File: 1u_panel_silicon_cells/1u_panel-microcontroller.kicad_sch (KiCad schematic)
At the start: 33 parts, among them J2 2-1734592-0, U1 TCAN330GDCNT, U11 TMP101NA/3KSLOTTED, U2 TMP101NA/3KSLOTTED, U7 STM32F091CCT7, X1 ECS-160-10-36Q-ES-TR

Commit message: changes for silicon solar module bringup tasks
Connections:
- net 3.3V: now also U11.4 (V+), U11.5 (ADD0), U2.4 (V+); no longer U11.1 (V+), U11.2 (ADD0), U2.1 (V+)
- net GND: now also U11.2 (GND); no longer U11.5 (GND)
- net SCL: now also U11.1 (SCL), U2.1 (SCL); no longer U11.4 (SCL), U2.4 (SCL)
- net SDA: now also U11.6 (SDA), U2.6 (SDA); no longer U11.3 (SDA), U2.3 (SDA)
- net at TP4.1: now also U2.3 (ALERT); no longer U2.6 (ALERT)
- net at TP30.1: now also U11.3 (ALERT); no longer U11.6 (ALERT)

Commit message: chages for https://github.com/oresat/oresat-solar-hardware/issues/53
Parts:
- U1: footprint oresat-ics:SOT23-8_TI-DCN -> Package_TO_SOT_SMD:SOT-23-8
- U11, U2: symbol oresat-ics:TMP101NA -> Sensor_Temperature:TMP101
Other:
- moved on the sheet: TP30, TP4

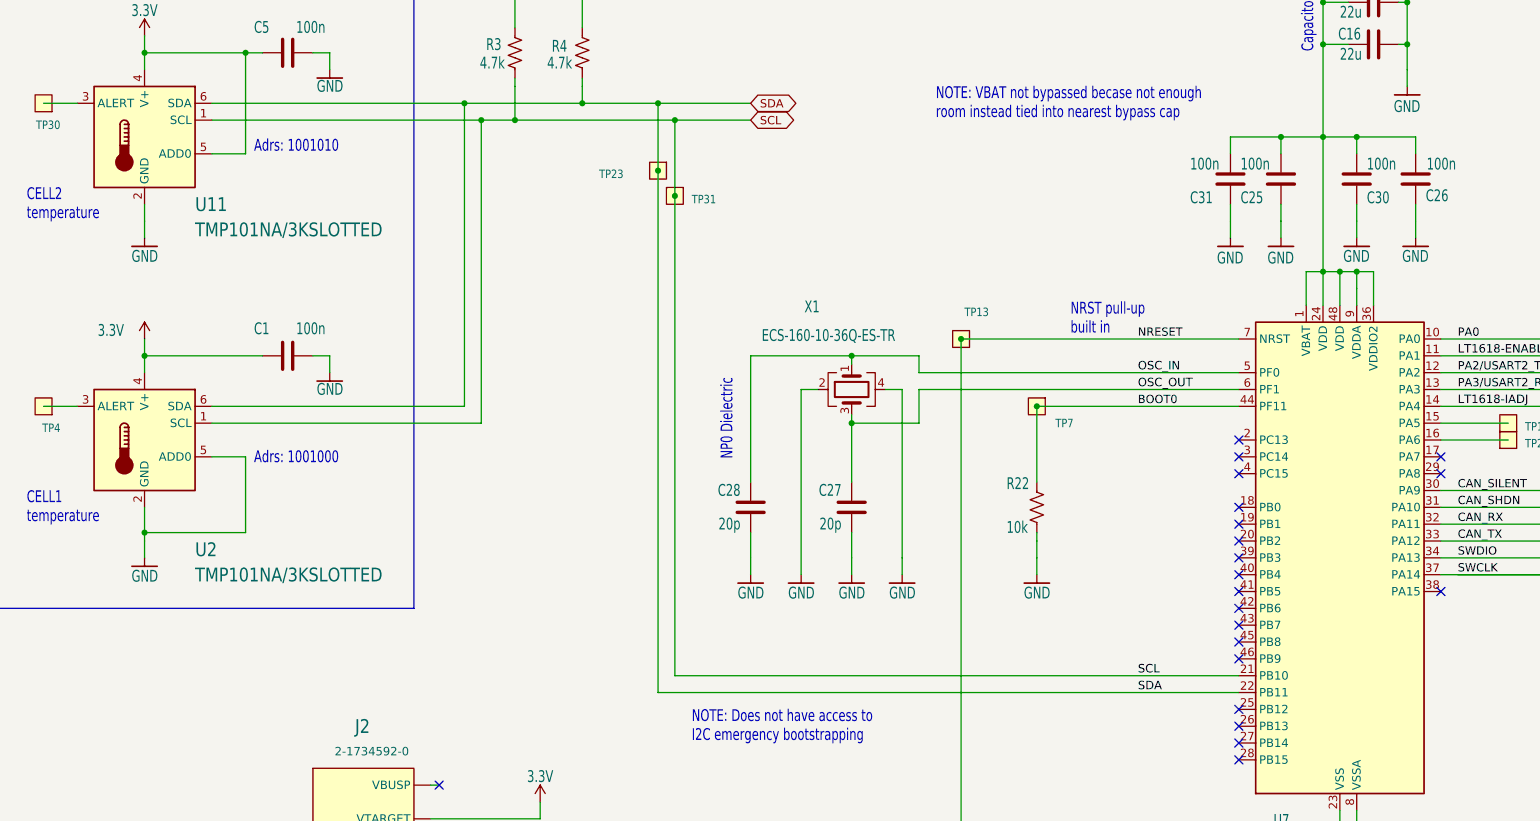
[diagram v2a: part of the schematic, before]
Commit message: changes for bringup issues on Si Solar module
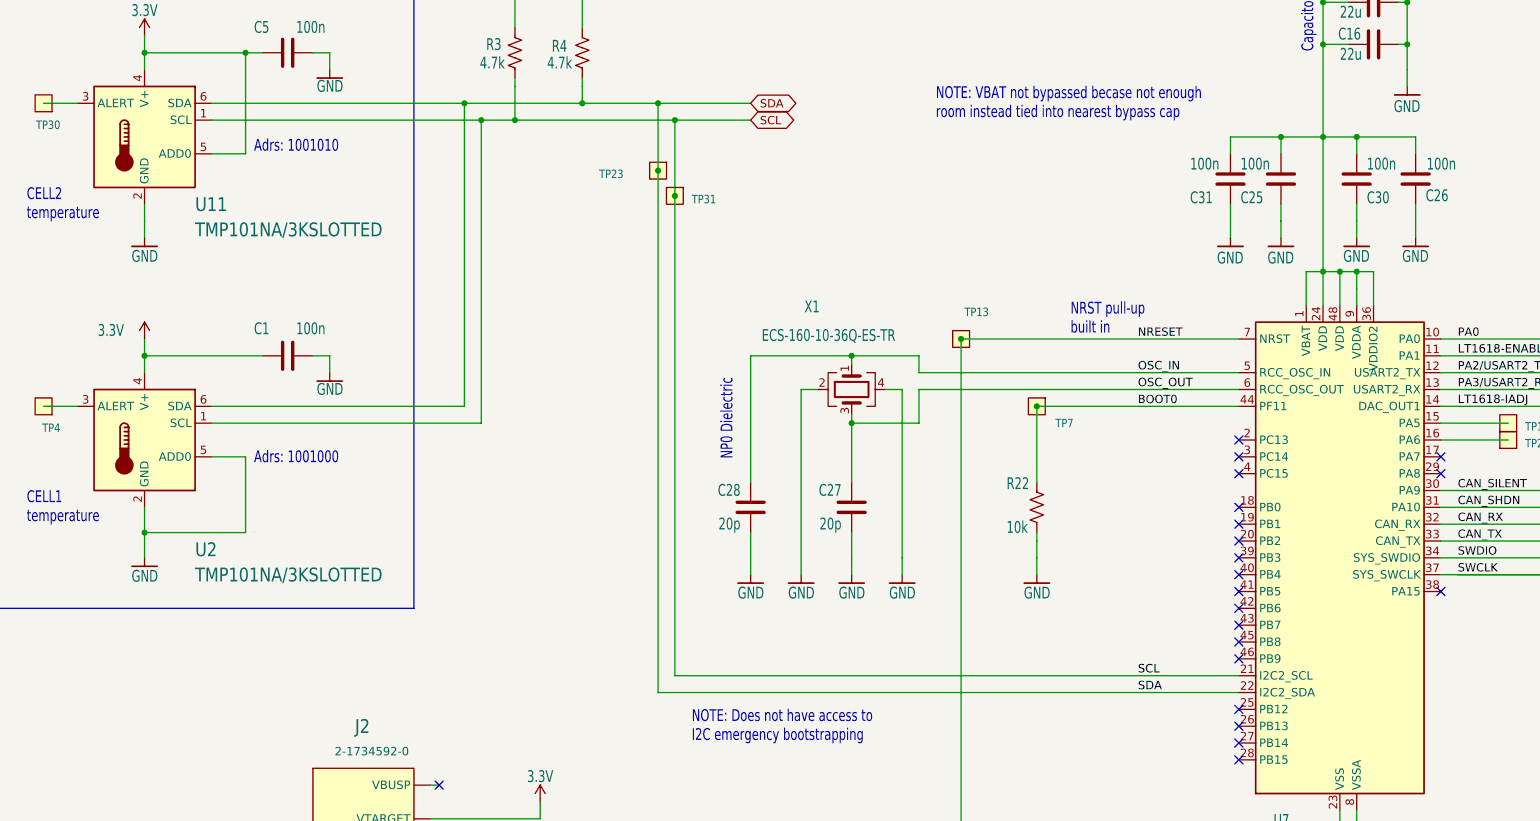
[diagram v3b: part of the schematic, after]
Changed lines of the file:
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@@
 (kicad_sch
-	(version 20231120)
+	(version 20250114)
 	(generator "eeschema")
-	(generator_version "8.0")
+	(generator_version "9.0")
 	(paper "USLedger")
 	(title_block
@@
 		(rev "1.0")
 	)
+	(text "Capacitor bank"
+		(exclude_from_sim no)
+		(at 243.84 50.8 90)
+		(effects
+			(font
+				(size 1.778 1.27)
+			)
+			(justify left bottom)
+		)
+	)
+	(text "Temp Sensors"
+		(exclude_from_sim no)
+		(at 58.42 38.1 0)
+		(effects
+			(font
+				(size 3.81 3.2385)
+				(thickness 0.6477)
+				(bold yes)
+			)
+			(justify left bottom)
+		)
+	)
+	(text "NOTE: VBAT not bypassed becase not enough\nroom instead tied into nearest bypass cap"
+		(exclude_from_sim no)
+		(at 186.69 60.96 0)
+		(effects
+			(font
+				(size 1.778 1.27)
+			)
+			(justify left bottom)
+		)
+	)
+	(text "DNP\nFOR\nFLIGHT"
+		(exclude_from_sim no)
+		(at 318.008 105.156 0)
+		(effects
+			(font
+				(size 1.778 1.27)
+			)
+			(justify left bottom)
+		)
+	)
+	(text "NRST pull-up\nbuilt in"
+		(exclude_from_sim no)
+		(at 207.01 93.472 0)
+		(effects
+			(font
+				(size 1.778 1.27)
+			)
+			(justify left bottom)
+		)
+	)
+	(text "DNP\nFOR\nFLIGHT"
+		(exclude_from_sim no)
+		(at 302.26 91.44 0)
+		(effects
+			(font
+				(size 1.778 1.27)
+			)
+			(justify left bottom)
+		)
+	)
+	(text "CAN Transceiver"
+		(exclude_from_sim no)
+		(at 365.76 88.9 0)
+		(effects
+			(font
+				(size 2.54 2.159)
+				(thickness 0.4318)
+				(bold yes)
+			)
+			(justify right bottom)
+		)
+	)
+	(text "NP0 Dielectric"
+		(exclude_from_sim no)
+		(at 156.21 112.268 90)
+		(effects
+			(font
+				(size 1.778 1.27)
+			)
+			(justify left bottom)
+		)
+	)
+	(text "NOTE: DEBUG-1 powers solar module\n3.3V directly from FT23X's onboard\nLDO on the DEBUG board. Schottky\ndiode drops 3.3V LDO output to 3.0V;\nkicking in solar should be  fine since\n3.3 V > 3.0V which the diode will\nblock."
+		(exclude_from_sim no)
+		(at 134.62 210.82 0)
+		(effects
+			(font
+				(size 1.778 1.27)
+			)
+			(justify left bottom)
+		)
+	)
+	(text "Adrs: 1001010"
+		(exclude_from_sim no)
+		(at 83.82 66.04 0)
+		(effects
+			(font
+				(size 1.778 1.27)
+			)
+			(justify left bottom)
+		)
+	)
+	(text "Adrs: 1001000"
+		(exclude_from_sim no)
+		(at 83.82 113.03 0)
+		(effects
+			(font
+				(size 1.778 1.27)
+			)
+			(justify left bottom)
+		)
+	)
+	(text "CELL2\ntemperature"
+		(exclude_from_sim no)
+		(at 49.53 76.2 0)
+		(effects
+			(font
+				(size 1.778 1.27)
+			)
+			(justify left bottom)
+		)
+	)
+	(text "RX-TX cross on\nDEBUG board"
+		(exclude_from_sim no)
+		(at 72.39 186.69 0)
+		(effects
+			(font
+				(size 1.778 1.27)
+			)
+			(justify left bottom)
+		)
+	)
+	(text "NOTE: Does not have access to\nI2C emergency bootstrapping"
+		(exclude_from_sim no)
+		(at 149.86 154.94 0)
+		(effects
+			(font
+				(size 1.778 1.27)
+			)
+			(justify left bottom)
+		)
+	)
+	(text "CELL1\ntemperature"
+		(exclude_from_sim no)
+		(at 49.53 121.92 0)
+		(effects
+			(font
+				(size 1.778 1.27)
+			)
+			(justify left bottom)
+		)
+	)
+	(text "0805"
+		(exclude_from_sim no)
+		(at 120.65 213.36 0)
+		(effects
+			(font
+				(size 1.778 1.27)
+			)
+			(justify left bottom)
+		)
+	)
 	(junction
 		(at 257.81 43.18)
@@
 		)
 	)
-	(text "Capacitor bank"
-		(exclude_from_sim no)
-		(at 243.84 50.8 90)
-		(effects
-			(font
-				(size 1.778 1.27)
-			)
-			(justify left bottom)
-		)
-	)
-	(text "Temp Sensors"
-		(exclude_from_sim no)
-		(at 58.42 38.1 0)
-		(effects
-			(font
-				(size 3.81 3.2385)
-				(thickness 0.6477)
-				(bold yes)
-			)
-			(justify left bottom)
-		)
-	)
-	(text "NOTE: VBAT not bypassed becase not enough\nroom instead tied into nearest bypass cap"
-		(exclude_from_sim no)
-		(at 186.69 60.96 0)
-		(effects
-			(font
-				(size 1.778 1.27)
-			)
-			(justify left bottom)
-		)
-	)
-	(text "DNP\nFOR\nFLIGHT"
-		(exclude_from_sim no)
-		(at 318.008 105.156 0)
-		(effects
-			(font
-				(size 1.778 1.27)
-			)
-			(justify left bottom)
-		)
-	)
-	(text "NRST pull-up\nbuilt in"
-		(exclude_from_sim no)
-		(at 207.01 93.472 0)
-		(effects
-			(font
-				(size 1.778 1.27)
-			)
-			(justify left bottom)
-		)
-	)
-	(text "DNP\nFOR\nFLIGHT"
-		(exclude_from_sim no)
-		(at 302.26 91.44 0)
-		(effects
-			(font
-				(size 1.778 1.27)
-			)
-			(justify left bottom)
-		)
-	)
-	(text "CAN Transceiver"
-		(exclude_from_sim no)
-		(at 365.76 88.9 0)
-		(effects
-			(font
-				(size 2.54 2.159)
-				(thickness 0.4318)
-				(bold yes)
-			)
-			(justify right bottom)
-		)
-	)
-	(text "NP0 Dielectric"
-		(exclude_from_sim no)
-		(at 156.21 112.268 90)
-		(effects
-			(font
-				(size 1.778 1.27)
-			)
-			(justify left bottom)
-		)
-	)
-	(text "NOTE: DEBUG-1 powers solar module\n3.3V directly from FT23X's onboard\nLDO on the DEBUG board. Schottky\ndiode drops 3.3V LDO output to 3.0V;\nkicking in solar should be  fine since\n3.3 V > 3.0V which the diode will\nblock."
-		(exclude_from_sim no)
-		(at 134.62 210.82 0)
-		(effects
-			(font
-				(size 1.778 1.27)
-			)
-			(justify left bottom)
-		)
-	)
-	(text "Adrs: 1001010"
-		(exclude_from_sim no)
-		(at 83.82 66.04 0)
-		(effects
-			(font
-				(size 1.778 1.27)
-			)
-			(justify left bottom)
-		)
-	)
-	(text "Adrs: 1001000"
-		(exclude_from_sim no)
-		(at 83.82 113.03 0)
-		(effects
-			(font
-				(size 1.778 1.27)
-			)
-			(justify left bottom)
-		)
-	)
-	(text "CELL2\ntemperature"
-		(exclude_from_sim no)
-		(at 49.53 76.2 0)
-		(effects
-			(font
-				(size 1.778 1.27)
-			)
-			(justify left bottom)
-		)
-	)
-	(text "RX-TX cross on\nDEBUG board"
-		(exclude_from_sim no)
-		(at 72.39 186.69 0)
-		(effects
-			(font
-				(size 1.778 1.27)
-			)
-			(justify left bottom)
-		)
-	)
-	(text "NOTE: Does not have access to\nI2C emergency bootstrapping"
-		(exclude_from_sim no)
-		(at 149.86 154.94 0)
-		(effects
-			(font
-				(size 1.778 1.27)
-			)
-			(justify left bottom)
-		)
-	)
-	(text "CELL1\ntemperature"
-		(exclude_from_sim no)
-		(at 49.53 121.92 0)
-		(effects
-			(font
-				(size 1.778 1.27)
-			)
-			(justify left bottom)
-		)
-	)
-	(text "0805"
-		(exclude_from_sim no)
-		(at 120.65 213.36 0)
-		(effects
-			(font
-				(size 1.778 1.27)
-			)
-			(justify left bottom)
-		)
-	)
 	(label "CAN_TX"
 		(at 265.43 124.46 0)
@@
 		(mirror x)
 		(unit 1)
-		(exclude_from_sim yes)
+		(exclude_from_sim no)
 		(in_bom no)
 		(on_board yes)
@@
 		(mirror y)
 		(unit 1)
-		(exclude_from_sim yes)
+		(exclude_from_sim no)
 		(in_bom no)
 		(on_board yes)
@@
 		(mirror x)
 		(unit 1)
-		(exclude_from_sim yes)
+		(exclude_from_sim no)
 		(in_bom no)
 		(on_board yes)
@@
 		(mirror y)
 		(unit 1)
-		(exclude_from_sim yes)
+		(exclude_from_sim no)
 		(in_bom no)
 		(on_board yes)
@@
 		)
 		(pin "12"
+			(alternate "USART2_TX")
 		)
 		(pin "13"
+			(alternate "USART2_RX")
 		)
 		(pin "14"
+			(alternate "DAC_OUT1")
 		)
 		(pin "15"
@@
 		)
 		(pin "21"
+			(alternate "I2C2_SCL")
 		)
 		(pin "22"
+			(alternate "I2C2_SDA")
 		)
 		(pin "23"
@@
 		)
 		(pin "32"
+			(alternate "CAN_RX")
 		)
 		(pin "33"
+			(alternate "CAN_TX")
 		)
 		(pin "34"
+			(alternate "SYS_SWDIO")
 		)
 		(pin "35"
@@
 		)
 		(pin "37"
+			(alternate "SYS_SWCLK")
 		)
 		(pin "38"
@@
 		)
 		(pin "5"
+			(alternate "RCC_OSC_IN")
 		)
 		(pin "6"
+			(alternate "RCC_OSC_OUT")
 		)
 		(pin "7"
@@
 		(at 52.07 104.14 180)
 		(unit 1)
-		(exclude_from_sim yes)
+		(exclude_from_sim no)
 		(in_bom no)
 		(on_board yes)
@@
 			)
 		)
-		(property "Description" "Amber 605nm LED Indication - Discrete 2V 0603 (1608 Metric)"
+		(property "Description" "Light emitting diode"
 			(at 314.96 99.06 0)
 			(effects
@@
 			)
 		)
+		(property "Sim.Pins" "1=K 2=A"
+			(at 314.96 99.06 0)
+			(effects
+				(font
+					(size 1.27 1.27)
+				)
+				(hide yes)
+			)
+		)
 		(pin "1"
 		)
@@
 		(mirror y)
 		(unit 1)
-		(exclude_from_sim yes)
+		(exclude_from_sim no)
 		(in_bom no)
 		(on_board yes)
@@
 		(at 52.07 58.42 180)
 		(unit 1)
-		(exclude_from_sim yes)
+		(exclude_from_sim no)
 		(in_bom no)
 		(on_board yes)
@@
 		(mirror y)
 		(unit 1)
-		(exclude_from_sim yes)
+		(exclude_from_sim no)
 		(in_bom no)
 		(on_board yes)

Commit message: Cleanup before fab! Added pullup resistors to ALERTs on TMP101s, removed some paranoia hardware including test points and pullups we don't need, did some schematic polishing for prettiness, and cleaned up some of the zones onthe layout. Removed the need for any old import or local symbol or footprint libraries. Upgraded to v1.1.
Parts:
- removed TP30, TP4: TEST-POINT-LARGE-SQUARE, oresat-misc:TestPoint-0.75mm-th, symbol oresat-misc:Test-Point-0.75mm-th
- removed U1: TCAN330GDCNT, Package_TO_SOT_SMD:SOT-23-8, symbol oresat-ics:TCAN330
- added R24, R25: 10k, oresat-passives:0603-C-NOSILK, symbol Device:R_US
- added U1: TCAN330, Package_TO_SOT_SMD:SOT-23-8, symbol Interface_CAN_LIN:TCAN330
- C1, C11, C16, C25, C26, C27, C28, C29, C3, C30, C31, C5, C9, J2, R15, R22, R23, R3, R4, U11, U2, X1: Distributor Digi-Key -> (none)
- D6: footprint oresat-diodes:LED-0603 -> LED_SMD:LED_0603_1608Metric; symbol Device:LED -> Device:LED_Small_Filled; Distributor Digi-Key -> (none)
- U7: symbol MCU_ST_STM32F0:STM32F091CCUx -> MCU_ST_STM32F0:STM32F091CCTx; Distributor Digi-Key -> (none)
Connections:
- net 3.3V: now also R24.2, R25.2, U1.3 (VCC)
- net CANH: now also U1.7 (CANH)
- net CANL: now also U1.6 (CANL)
- net CAN_RX: now also U1.4 (RXD)
- net CAN_SHDN: now also U1.5 (SHDN)
- net CAN_SILENT: now also U1.8 (S)
- net CAN_TX: now also U1.1 (TXD)
- net GND: now also U1.2 (GND); no longer U7.49 (VSS)
- net INA226-nALERT: now reaches U7.20 (PB2)
- net at U7.39 (PB3): now also U11.3 (ALERT), R25.1
- net at U7.40 (PB4): now also U2.3 (ALERT), R24.1
- no-connect marks 29 -> 26
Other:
- note added: "All caps are ceramic 10% X5R >= 16V Vwv and AEQ unless marked"
- note added: "All resistors 0603 +/- 1% and AEQ unless marked"
- note added: "EXTREMELY IMPORTANT ALL COMPONENTS ON TOP LAYER MUST BE < 2 MM TALL ALL COMPONENTS ON TOP LAYER WITH FASTENERS BELOW THEM MUST BE < 0.7 MM TALL CHECK USER.DRAWINGS LAYER FOR FASTNER PLACEMENT"
- note added: "SCL"
- note added: "SDA"
- note removed: "NOTE: Does not have access to I2C emergency bootstrapping"
- moved on the sheet: C1, C27, C28, C29, C5, J2, R15, R22, R23, R3, R4, TP23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
